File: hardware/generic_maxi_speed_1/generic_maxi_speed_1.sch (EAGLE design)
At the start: 31 parts, among them IC1 MEGA168/328, IC2 RFM12, IC3 LP2950Z, Q1 20MHz

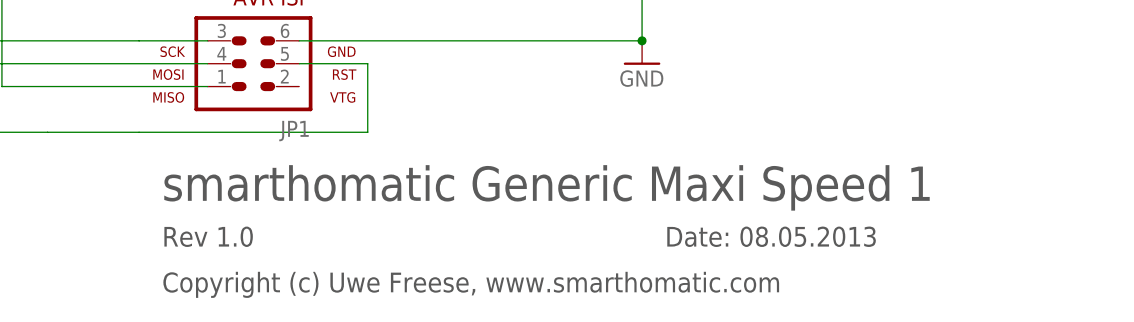
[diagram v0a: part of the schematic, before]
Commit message: use .org domain
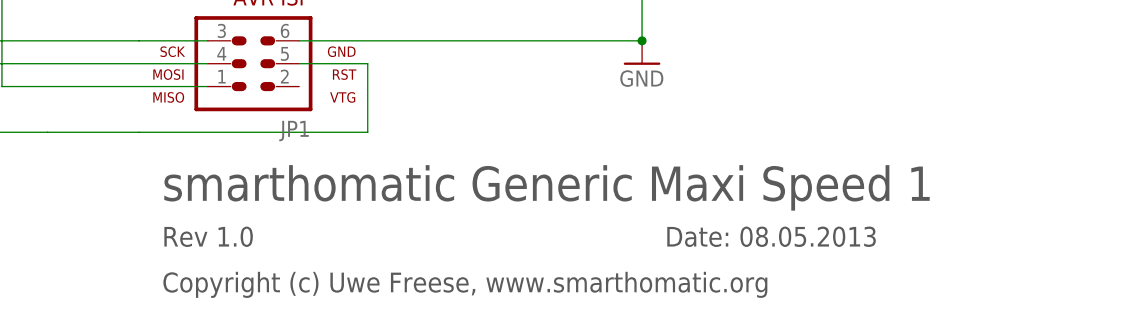
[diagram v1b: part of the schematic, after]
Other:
- note added: "Copyright (c) Uwe Freese, www.smarthomatic.org"
- note removed: "Copyright (c) Uwe Freese, www.smarthomatic.com"
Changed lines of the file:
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@@
 <text x="121.92" y="-45.72" size="2.1844" layer="97">Date: 08.05.2013</text>
 <text x="66.04" y="-45.72" size="2.1844" layer="97">Rev 1.0</text>
-<text x="66.04" y="-50.8" size="2.1844" layer="97">Copyright (c) Uwe Freese, www.smarthomatic.com</text>
+<text x="66.04" y="-50.8" size="2.1844" layer="97">Copyright (c) Uwe Freese, www.smarthomatic.org</text>
 </plain>
 <instances>

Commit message: add holes
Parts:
- D1: value 1N4148DO35-7 -> 1N4148
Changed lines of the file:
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@@
 <part name="JP2" library="pinhead" deviceset="PINHD-1X1" device="" value="ANT"/>
 <part name="IC3" library="linear" deviceset="LP2950" device="Z"/>
-<part name="D1" library="diode" deviceset="1N4148" device="DO35-7"/>
+<part name="D1" library="diode" deviceset="1N4148" device="DO35-7" value="1N4148"/>
 <part name="+3V1" library="supply1" deviceset="+3V3" device=""/>
 <part name="P+4" library="supply1" deviceset="+5V" device=""/>

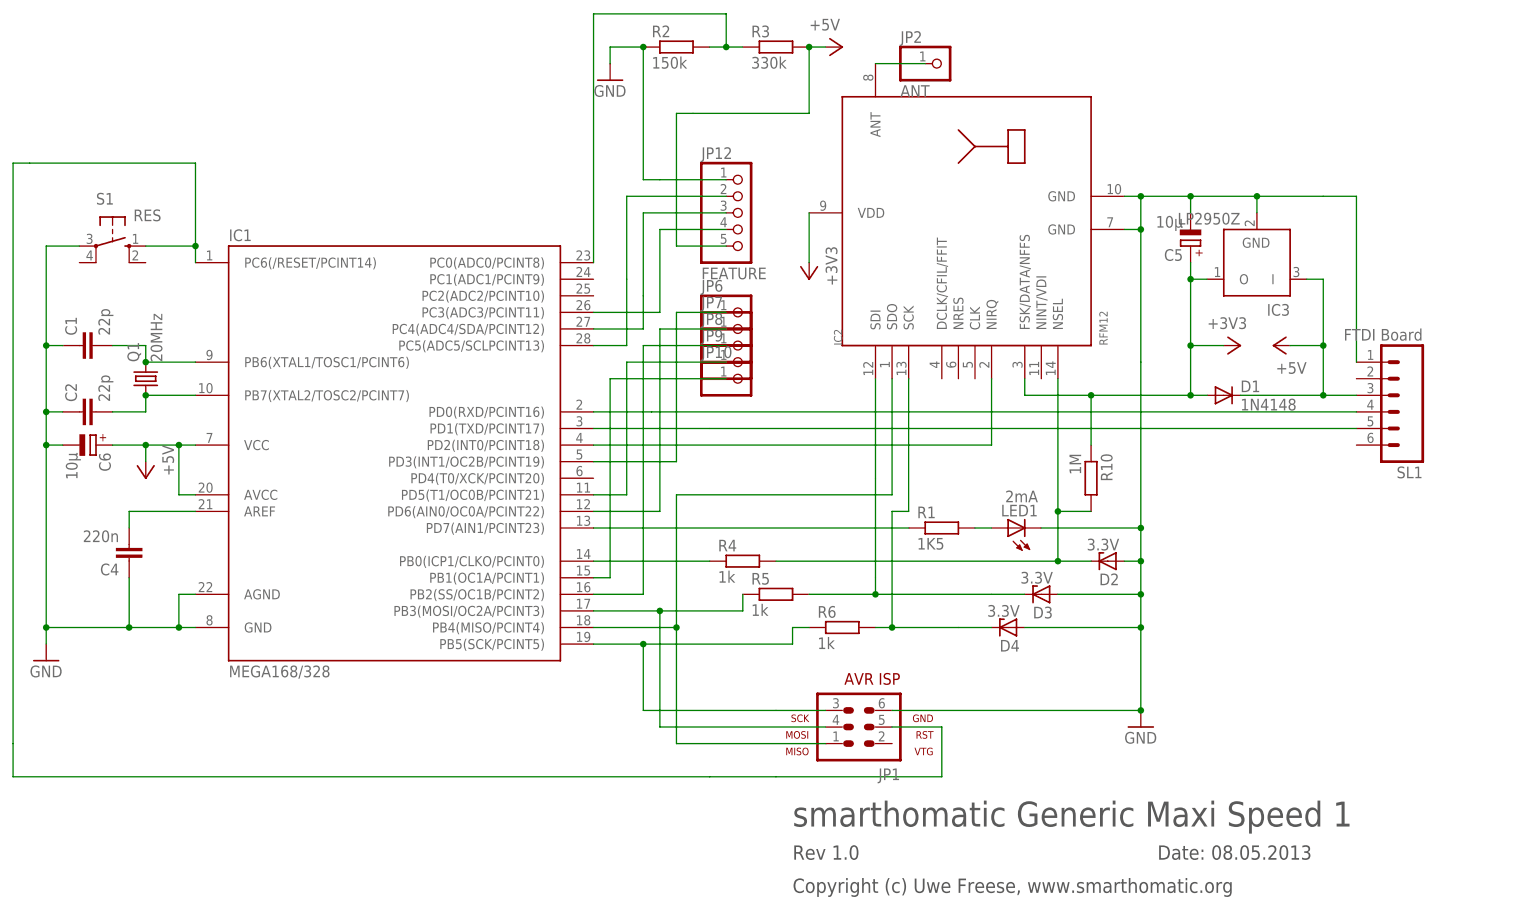
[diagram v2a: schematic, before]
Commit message: Generic Maxi Speed V1.1 includes a solder switch to turn on the VCC pin of the ISP connector.
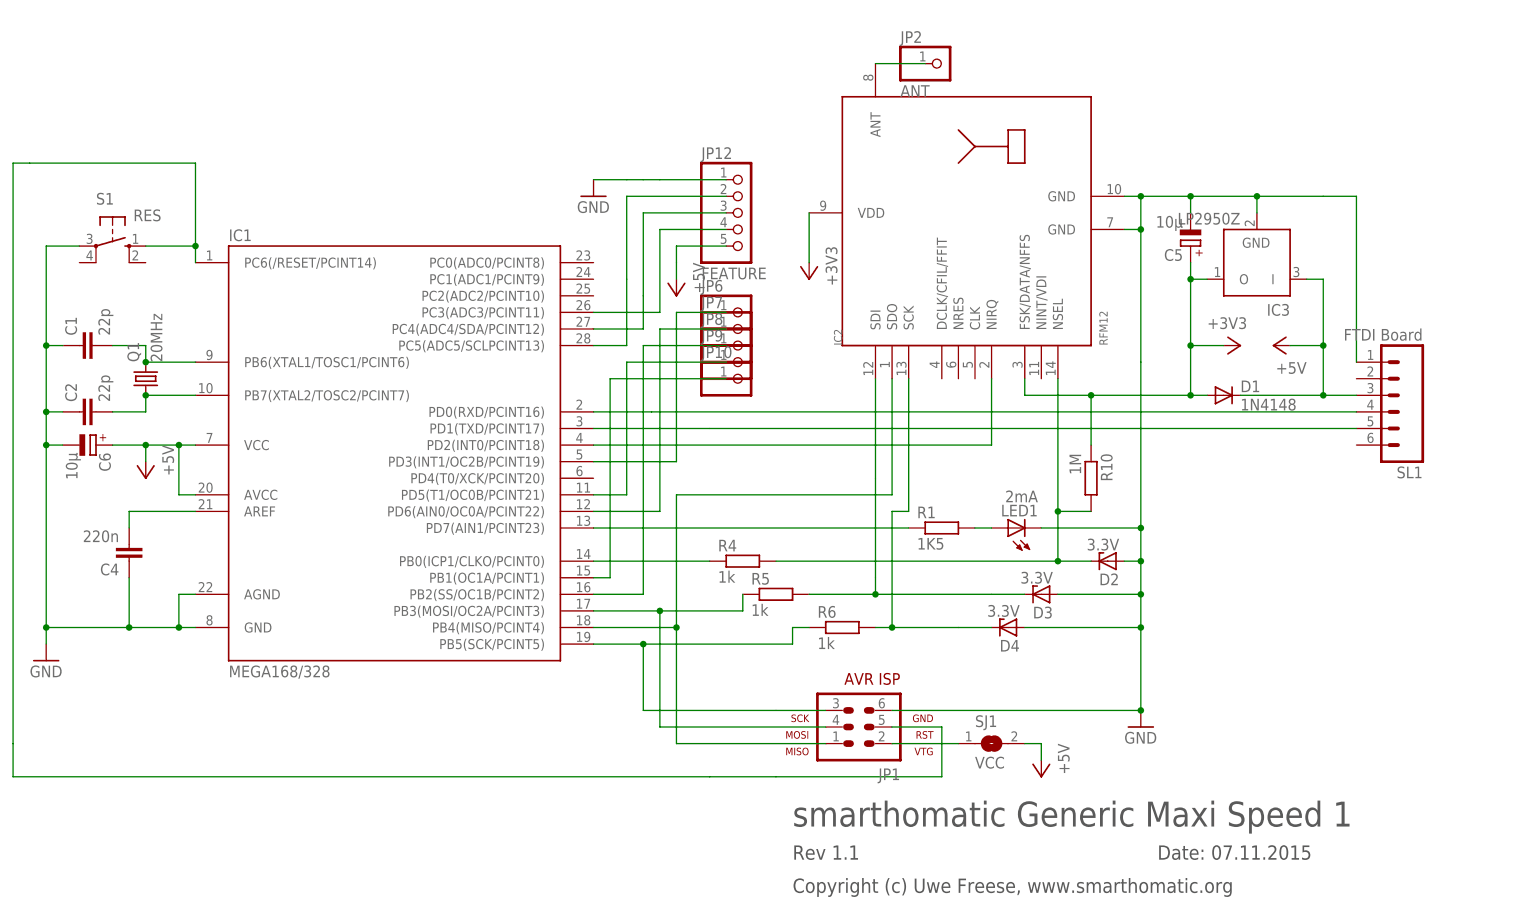
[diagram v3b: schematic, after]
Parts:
- removed R2: 150k, rcl:R-EU_0207/7
- removed R3: 330k, rcl:R-EU_0207/7
- added SJ1: VCC, jumper:SJ
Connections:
- net +5V: now also SJ1.2; no longer R3.2
- net GND: no longer R2.1
- net N$18: now also JP1.2, SJ1.1; no longer IC1.PC0(ADC0/PCINT8), R2.2, R3.1
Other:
- note added: "Date: 07.11.2015"
- note added: "Rev 1.1"
- note removed: "Date: 08.05.2013"
- note removed: "Rev 1.0"
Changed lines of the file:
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@@
 <?xml version="1.0" encoding="utf-8"?>
 <!DOCTYPE eagle SYSTEM "eagle.dtd">
-<eagle version="6.4">
+<eagle version="7.3.0">
 <drawing>
 <settings>
@@
 <part name="C5" library="rcl" deviceset="CPOL-EU" device="E1.8-4" value="10µ"/>
 <part name="SL1" library="con-amp-quick" deviceset="M06" device="" value="FTDI Board"/>
-<part name="R2" library="rcl" deviceset="R-EU_" device="0207/7" value="150k"/>
-<part name="R3" library="rcl" deviceset="R-EU_" device="0207/7" value="330k"/>
 <part name="GND3" library="supply1" deviceset="GND" device=""/>
 <part name="R10" library="rcl" deviceset="R-EU_" device="0207/7" value="1M"/>
@@
 <part name="D3" library="diode" deviceset="ZENER-DIODE" device="ZD-5" value="3.3V"/>
 <part name="D4" library="diode" deviceset="ZENER-DIODE" device="ZD-5" value="3.3V"/>
+<part name="SJ1" library="jumper" deviceset="SJ" device="" value="VCC"/>
+<part name="P+3" library="supply1" deviceset="+5V" device=""/>
 </parts>
 <sheets>
@@
 <frame x1="-60.96" y1="-58.42" x2="172.72" y2="93.98" columns="8" rows="5" layer="97"/>
 <text x="66.04" y="-40.64" size="3.81" layer="97">smarthomatic Generic Maxi Speed 1</text>
-<text x="121.92" y="-45.72" size="2.1844" layer="97">Date: 08.05.2013</text>
-<text x="66.04" y="-45.72" size="2.1844" layer="97">Rev 1.0</text>
+<text x="121.92" y="-45.72" size="2.1844" layer="97">Date: 07.11.2015</text>
+<text x="66.04" y="-45.72" size="2.1844" layer="97">Rev 1.1</text>
 <text x="66.04" y="-50.8" size="2.1844" layer="97">Copyright (c) Uwe Freese, www.smarthomatic.org</text>
 </plain>
@@
 <attribute name="NAME" x="162.56" y="14.478" size="1.778" layer="95" rot="R180"/>
 </instance>
-<instance part="R2" gate="G$1" x="48.26" y="78.74"/>
-<instance part="R3" gate="G$1" x="63.5" y="78.74"/>
-<instance part="GND3" gate="1" x="38.1" y="73.66"/>
+<instance part="GND3" gate="1" x="35.56" y="55.88"/>
 <instance part="R10" gate="G$1" x="111.76" y="12.7" rot="R270"/>
 <instance part="C1" gate="G$1" x="-43.18" y="33.02" rot="R90"/>
@@
 <instance part="P+1" gate="1" x="139.7" y="33.02" rot="R90"/>
 <instance part="+3V3" gate="G$1" x="134.62" y="33.02" rot="R270"/>
-<instance part="P+2" gate="1" x="73.66" y="78.74" rot="R270"/>
+<instance part="P+2" gate="1" x="48.26" y="40.64" rot="R180"/>
 <instance part="R5" gate="G$1" x="63.5" y="-5.08"/>
 <instance part="R6" gate="G$1" x="73.66" y="-10.16"/>
@@
 <instance part="D3" gate="G$1" x="104.14" y="-5.08" rot="R180"/>
 <instance part="D4" gate="G$1" x="99.06" y="-10.16" rot="R180"/>
+<instance part="SJ1" gate="1" x="96.52" y="-27.94"/>
+<instance part="P+3" gate="1" x="104.14" y="-33.02" rot="R180"/>
 </instances>
 <busses>
@@
 </segment>
 <segment>
-<pinref part="R2" gate="G$1" pin="1"/>
 <pinref part="GND3" gate="1" pin="GND"/>
-<wire x1="43.18" y1="78.74" x2="38.1" y2="78.74" width="0.1524" layer="91"/>
-<wire x1="38.1" y1="78.74" x2="38.1" y2="76.2" width="0.1524" layer="91"/>
-<wire x1="43.18" y1="78.74" x2="43.18" y2="58.42" width="0.1524" layer="91"/>
-<junction x="43.18" y="78.74"/>
+<wire x1="40.64" y1="58.42" x2="35.56" y2="58.42" width="0.1524" layer="91"/>
+<wire x1="40.64" y1="58.42" x2="43.18" y2="58.42" width="0.1524" layer="91"/>
 <wire x1="43.18" y1="58.42" x2="45.72" y2="58.42" width="0.1524" layer="91"/>
 <pinref part="JP12" gate="A" pin="1"/>
@@
 <pinref part="IC2" gate="G$1" pin="NIRQ"/>
 <wire x1="96.52" y1="17.78" x2="96.52" y2="27.94" width="0.1524" layer="91"/>
-</segment>
-</net>
-<net name="N$18" class="0">
-<segment>
-<pinref part="R3" gate="G$1" pin="1"/>
-<pinref part="R2" gate="G$1" pin="2"/>
-<wire x1="58.42" y1="78.74" x2="55.88" y2="78.74" width="0.1524" layer="91"/>
-<pinref part="IC1" gate="1" pin="PC0(ADC0/PCINT8)"/>
-<wire x1="55.88" y1="78.74" x2="53.34" y2="78.74" width="0.1524" layer="91"/>
-<wire x1="35.56" y1="45.72" x2="35.56" y2="83.82" width="0.1524" layer="91"/>
-<wire x1="35.56" y1="83.82" x2="55.88" y2="83.82" width="0.1524" layer="91"/>
-<wire x1="55.88" y1="83.82" x2="55.88" y2="78.74" width="0.1524" layer="91"/>
-<junction x="55.88" y="78.74"/>
 </segment>
 </net>
@@
 </segment>
 <segment>
-<pinref part="R3" gate="G$1" pin="2"/>
-<wire x1="68.58" y1="78.74" x2="68.58" y2="68.58" width="0.1524" layer="91"/>
-<wire x1="50.8" y1="68.58" x2="68.58" y2="68.58" width="0.1524" layer="91"/>
 <pinref part="P+2" gate="1" pin="+5V"/>
-<wire x1="68.58" y1="78.74" x2="71.12" y2="78.74" width="0.1524" layer="91"/>
-<junction x="68.58" y="78.74"/>
+<wire x1="48.26" y1="45.72" x2="48.26" y2="43.18" width="0.1524" layer="91"/>
 <pinref part="JP12" gate="A" pin="5"/>
 <wire x1="55.88" y1="48.26" x2="48.26" y2="48.26" width="0.1524" layer="91"/>
-<wire x1="48.26" y1="48.26" x2="48.26" y2="68.58" width="0.1524" layer="91"/>
-<wire x1="48.26" y1="68.58" x2="50.8" y2="68.58" width="0.1524" layer="91"/>
+<wire x1="48.26" y1="48.26" x2="48.26" y2="45.72" width="0.1524" layer="91"/>
+</segment>
+<segment>
+<pinref part="SJ1" gate="1" pin="2"/>
+<pinref part="P+3" gate="1" pin="+5V"/>
+<wire x1="101.6" y1="-27.94" x2="104.14" y2="-27.94" width="0.1524" layer="91"/>
+<wire x1="104.14" y1="-27.94" x2="104.14" y2="-30.48" width="0.1524" layer="91"/>
 </segment>
 </net>
@@
 </segment>
 </net>
+<net name="N$18" class="0">
+<segment>
+<pinref part="JP1" gate="G$1" pin="2"/>
+<pinref part="SJ1" gate="1" pin="1"/>
+<wire x1="81.28" y1="-27.94" x2="91.44" y2="-27.94" width="0.1524" layer="91"/>
+</segment>
+</net>
